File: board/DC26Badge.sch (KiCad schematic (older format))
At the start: 6 parts, among them U1 HT16K33-28

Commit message: Prototype schematic finished.
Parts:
- added C2: 4.7u, symbol DC26Badge-rescue:C_Small
- added C3, C4, C5: 0.1u, symbol DC26Badge-rescue:C_Small
- added D1, D2, D3: LED, symbol Device:LED
- added J1: PWR_HDR, symbol Connector_Generic:Conn_01x02
- added J2: PWR_CONN, symbol Connector_Generic:Conn_01x02
- added J3: VOLTMETER, symbol Connector_Generic:Conn_01x02
- added J4: AMMETER, symbol Connector_Generic:Conn_01x02
- added J5: Cortex_SWD, symbol Connector_Generic:Conn_02x05_Odd_Even
- added R1: 0.1, symbol Device:R_Shunt
- added R2, R3, R4, R5: 1k, symbol Device:R_Small
- added SW1: JOYSTICK, symbol dc26badge-custom:JOYSTICK
- added SW2: SW_Push, symbol Switch:SW_Push
- added TP1: PWRTP, symbol Connector_Specialized:Test_Point_2Pole
- added U2: BT832, symbol dc26badge-custom:BT832
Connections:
- net labels added: CTR, DN, LED1, LED2, LED3, LT, P_IN, RESET, RT, SWDCLK, SWDIO, UP
- wire segments 98 -> 183
- no-connect marks 1 -> 5
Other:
- moved on the sheet: C1

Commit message: First pass of prototype PCB layout.
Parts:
- removed D2, D3: LED, symbol Device:LED
- removed R4, R5: 1k, symbol Device:R_Small
- C2, C3, C4, C5: footprint (none) -> Capacitor_SMD:C_0603_1608Metric
- D1: footprint (none) -> LED_SMD:LED_0603_1608Metric
- J1, J3, J4: footprint (none) -> PinHeaders:Pin_Header_Straight_1x02_Pitch2.54mm
- J2: footprint (none) -> Connector_JST:JST_PH_S2B-PH-SM4-TB_1x02_P2.00mm_Horizontal
- J5: footprint (none) -> Connector_PinHeader_1.27mm:PinHeader_2x05_P1.27mm_Vertical_SMD
- R1: footprint (none) -> DC26badge:FC4T
- R2, R3: footprint (none) -> Resistor_SMD:R_0603_1608Metric
- SW1: footprint (none) -> DC26badge:JOYSTICK
- SW2: footprint (none) -> Button_Switch_SMD:SW_SPST_SKQG
- TP1: footprint (none) -> TestPoint:TestPoint_2Pads_Pitch2.54mm_Drill0.8mm
- U2: footprint (none) -> DC26badge:BT832
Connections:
- net labels removed: LED2, LED3
- wire segments 183 -> 173
- no-connect marks 5 -> 7
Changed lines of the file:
@@
 F 0 "U2" H 4500 3900 50  0000 C CNN
 F 1 "BT832" H 4025 5124 50  0000 C CNN
-F 2 "" H 3850 4050 50  0001 C CNN
+F 2 "DC26badge:BT832" H 3850 4050 50  0001 C CNN
 F 3 "" H 3850 4050 50  0001 C CNN
 	1    4050 4050
@@
 F 0 "J5" H 6850 3767 50  0000 C CNN
 F 1 "Cortex_SWD" H 6850 3676 50  0000 C CNN
-F 2 "" H 6800 3350 50  0001 C CNN
+F 2 "Connector_PinHeader_1.27mm:PinHeader_2x05_P1.27mm_Vertical_SMD" H 6800 3350 50  0001 C CNN
 F 3 "~" H 6800 3350 50  0001 C CNN
 	1    6800 3350
@@
 F 0 "SW1" H 4500 4700 50  0000 C CNN
 F 1 "JOYSTICK" H 4050 5324 50  0000 C CNN
-F 2 "" H 4050 5000 50  0001 C CNN
+F 2 "DC26badge:JOYSTICK" H 4050 5000 50  0001 C CNN
 F 3 "" H 4050 5000 50  0001 C CNN
 	1    4050 5000
@@
 	5000 5100 4700 5100
 Text Label 3000 3400 0    50   ~ 0
+UP
+Text Label 3000 3500 0    50   ~ 0
 CTR
-Text Label 3000 3500 0    50   ~ 0
-UP
 Text Label 3000 3600 0    50   ~ 0
 DN
@@
 L Connector_Generic:Conn_01x02 J1
 U 1 1 5AFF7E7C
-P 950 1050
-F 0 "J1" H 870 725 50  0000 C CNN
-F 1 "PWR_HDR" H 870 816 50  0000 C CNN
-F 2 "" H 950 1050 50  0001 C CNN
-F 3 "~" H 950 1050 50  0001 C CNN
-	1    950  1050
-	-1   0    0    1
+P 950 950
+F 0 "J1" H 870 1167 50  0000 C CNN
+F 1 "PWR_HDR" H 870 1076 50  0000 C CNN
+F 2 "PinHeaders:Pin_Header_Straight_1x02_Pitch2.54mm" H 950 950 50  0001 C CNN
+F 3 "~" H 950 950 50  0001 C CNN
+	1    950  950
+	-1   0    0    -1
 $EndComp
 $Comp
 L Connector_Generic:Conn_01x02 J2
 U 1 1 5AFF7F88
-P 950 1700
-F 0 "J2" H 870 1375 50  0000 C CNN
-F 1 "PWR_CONN" H 870 1466 50  0000 C CNN
-F 2 "" H 950 1700 50  0001 C CNN
-F 3 "~" H 950 1700 50  0001 C CNN
-	1    950  1700
-	-1   0    0    1
+P 950 1600
+F 0 "J2" H 870 1817 50  0000 C CNN
+F 1 "PWR_CONN" H 870 1726 50  0000 C CNN
+F 2 "Connector_JST:JST_PH_S2B-PH-SM4-TB_1x02_P2.00mm_Horizontal" H 950 1600 50  0001 C CNN
+F 3 "~" H 950 1600 50  0001 C CNN
+	1    950  1600
+	-1   0    0    -1
 $EndComp
 $Comp
 L Connector_Generic:Conn_01x02 J3
 U 1 1 5AFF811D
-P 950 2300
-F 0 "J3" H 870 1975 50  0000 C CNN
-F 1 "VOLTMETER" H 870 2066 50  0000 C CNN
-F 2 "" H 950 2300 50  0001 C CNN
-F 3 "~" H 950 2300 50  0001 C CNN
-	1    950  2300
-	-1   0    0    1
+P 950 2200
+F 0 "J3" H 870 2417 50  0000 C CNN
+F 1 "VOLTMETER" H 870 2326 50  0000 C CNN
+F 2 "PinHeaders:Pin_Header_Straight_1x02_Pitch2.54mm" H 950 2200 50  0001 C CNN
+F 3 "~" H 950 2200 50  0001 C CNN
+	1    950  2200
+	-1   0    0    -1
 $EndComp
 $Comp
@@
 F 0 "J4" H 870 2625 50  0000 C CNN
 F 1 "AMMETER" H 870 2716 50  0000 C CNN
-F 2 "" H 950 2950 50  0001 C CNN
+F 2 "PinHeaders:Pin_Header_Straight_1x02_Pitch2.54mm" H 950 2950 50  0001 C CNN
 F 3 "~" H 950 2950 50  0001 C CNN
 	1    950  2950
@@
 F 0 "R1" H 1362 2904 50  0000 R CNN
 F 1 "0.1" H 1362 2995 50  0000 R CNN
-F 2 "" V 1380 2950 50  0001 C CNN
+F 2 "DC26badge:FC4T" V 1380 2950 50  0001 C CNN
 F 3 "~" H 1450 2950 50  0001 C CNN
 	1    1450 2950
@@
 F 0 "C2" H 2242 1046 50  0000 L CNN
 F 1 "4.7u" H 2242 955 50  0000 L CNN
-F 2 "" H 2150 1000 50  0001 C CNN
+F 2 "Capacitor_SMD:C_0603_1608Metric" H 2150 1000 50  0001 C CNN
 F 3 "" H 2150 1000 50  0001 C CNN
 	1    2150 1000
@@
 F 0 "C3" H 2542 1046 50  0000 L CNN
 F 1 "0.1u" H 2542 955 50  0000 L CNN
-F 2 "" H 2450 1000 50  0001 C CNN
+F 2 "Capacitor_SMD:C_0603_1608Metric" H 2450 1000 50  0001 C CNN
 F 3 "" H 2450 1000 50  0001 C CNN
 	1    2450 1000
@@
 F 0 "C4" H 2842 1046 50  0000 L CNN
 F 1 "0.1u" H 2842 955 50  0000 L CNN
-F 2 "" H 2750 1000 50  0001 C CNN
+F 2 "Capacitor_SMD:C_0603_1608Metric" H 2750 1000 50  0001 C CNN
 F 3 "" H 2750 1000 50  0001 C CNN
 	1    2750 1000
@@
 F 0 "SW2" H 1800 4435 50  0000 C CNN
 F 1 "SW_Push" H 1800 4344 50  0000 C CNN
-F 2 "" H 1800 4350 50  0001 C CNN
+F 2 "Button_Switch_SMD:SW_SPST_SKQG" H 1800 4350 50  0001 C CNN
 F 3 "" H 1800 4350 50  0001 C CNN
 	1    1800 4150
@@
 F 0 "C5" H 1392 4396 50  0000 L CNN
 F 1 "0.1u" H 1392 4305 50  0000 L CNN
-F 2 "" H 1300 4350 50  0001 C CNN
+F 2 "Capacitor_SMD:C_0603_1608Metric" H 1300 4350 50  0001 C CNN
 F 3 "" H 1300 4350 50  0001 C CNN
 	1    1300 4350
@@
 F 0 "R3" H 1359 3996 50  0000 L CNN
 F 1 "1k" H 1359 3905 50  0000 L CNN
-F 2 "" H 1300 3950 50  0001 C CNN
+F 2 "Resistor_SMD:R_0603_1608Metric" H 1300 3950 50  0001 C CNN
 F 3 "~" H 1300 3950 50  0001 C CNN
 	1    1300 3950
@@
 F 0 "D1" V 988 5233 50  0000 R CNN
 F 1 "LED" V 897 5233 50  0000 R CNN
-F 2 "" H 950 5350 50  0001 C CNN
+F 2 "LED_SMD:LED_0603_1608Metric" H 950 5350 50  0001 C CNN
 F 3 "~" H 950 5350 50  0001 C CNN
 	1    950  5350
@@
 $EndComp
 $Comp
-L Device:LED D2
-U 1 1 5B0E1889
-P 1300 5350
-F 0 "D2" V 1338 5233 50  0000 R CNN
-F 1 "LED" V 1247 5233 50  0000 R CNN
-F 2 "" H 1300 5350 50  0001 C CNN
-F 3 "~" H 1300 5350 50  0001 C CNN
-	1    1300 5350
-	0    -1   -1   0
-$EndComp
-$Comp
-L Device:LED D3
-U 1 1 5B0E19A7
-P 1600 5350
-F 0 "D3" V 1638 5233 50  0000 R CNN
-F 1 "LED" V 1547 5233 50  0000 R CNN
-F 2 "" H 1600 5350 50  0001 C CNN
-F 3 "~" H 1600 5350 50  0001 C CNN
-	1    1600 5350
-	0    -1   -1   0
-$EndComp
-$Comp
 L power:VDD #PWR0103
 U 1 1 5B0E1C02
-P 1300 5100
-F 0 "#PWR0103" H 1300 4950 50  0001 C CNN
-F 1 "VDD" H 1317 5273 50  0000 C CNN
-F 2 "" H 1300 5100 50  0001 C CNN
-F 3 "" H 1300 5100 50  0001 C CNN
-	1    1300 5100
+P 950 5100
+F 0 "#PWR0103" H 950 4950 50  0001 C CNN
+F 1 "VDD" H 967 5273 50  0000 C CNN
+F 2 "" H 950 5100 50  0001 C CNN
+F 3 "" H 950 5100 50  0001 C CNN
+	1    950  5100
 	1    0    0    -1
 $EndComp
 Wire Wire Line
 	950  5200 950  5100
-Wire Wire Line
-	950  5100 1300 5100
-Wire Wire Line
-	1300 5200 1300 5100
-Connection ~ 1300 5100
-Wire Wire Line
-	1300 5100 1600 5100
-Wire Wire Line
-	1600 5100 1600 5200
 $Comp
 L Device:R_Small R2
@@
 F 0 "R2" H 1009 5796 50  0000 L CNN
 F 1 "1k" H 1009 5705 50  0000 L CNN
-F 2 "" H 950 5750 50  0001 C CNN
+F 2 "Resistor_SMD:R_0603_1608Metric" H 950 5750 50  0001 C CNN
 F 3 "~" H 950 5750 50  0001 C CNN
 	1    950  5750
 	1    0    0    -1
 $EndComp
-$Comp
-L Device:R_Small R4
-U 1 1 5B1339BD
-P 1300 5750
-F 0 "R4" H 1359 5796 50  0000 L CNN
-F 1 "1k" H 1359 5705 50  0000 L CNN
-F 2 "" H 1300 5750 50  0001 C CNN
-F 3 "~" H 1300 5750 50  0001 C CNN
-	1    1300 5750
-	1    0    0    -1
-$EndComp
-$Comp
-L Device:R_Small R5
-U 1 1 5B133A7E
-P 1600 5750
-F 0 "R5" H 1659 5796 50  0000 L CNN
-F 1 "1k" H 1659 5705 50  0000 L CNN
-F 2 "" H 1600 5750 50  0001 C CNN
-F 3 "~" H 1600 5750 50  0001 C CNN
-	1    1600 5750
-	1    0    0    -1
-$EndComp
 Wire Wire Line
 	950  5650 950  5500
 Wire Wire Line
-	1300 5500 1300 5650
-Wire Wire Line
-	1600 5650 1600 5500
-Wire Wire Line
 	950  5850 950  6100
-Wire Wire Line
-	1300 6100 1300 5850
-Wire Wire Line
-	1600 5850 1600 6100
-Text Label 950  6100 0    50   ~ 0
-LED1
-Text Label 1300 6100 0    50   ~ 0
-LED2
-Text Label 1600 6100 0    50   ~ 0
-LED3
 NoConn ~ 3300 3900
 Wire Wire Line
 	4750 3500 5000 3500
-Wire Wire Line
-	4750 3600 5000 3600
-Wire Wire Line
-	4750 3700 5000 3700
 Text Label 5000 3500 2    50   ~ 0
 LED1
-Text Label 5000 3600 2    50   ~ 0
-LED2
-Text Label 5000 3700 2    50   ~ 0
-LED3
 $Comp
 L Connector_Specialized:Test_Point_2Pole TP1
@@
 F 0 "TP1" H 2450 2245 50  0000 C CNN
 F 1 "PWRTP" H 2450 2154 50  0000 C CNN
-F 2 "" H 2450 2050 50  0001 C CNN
+F 2 "TestPoint:TestPoint_2Pads_Pitch2.54mm_Drill0.8mm" H 2450 2050 50  0001 C CNN
 F 3 "~" H 2450 2050 50  0001 C CNN
 	1    2450 2050
@@
 	2850 2200 2850 2050
 Connection ~ 2850 2050
+$Comp
+L power:GND #PWR0104
+U 1 1 5B1EF48E
+P 6400 3700
+F 0 "#PWR0104" H 6400 3450 50  0001 C CNN
+F 1 "GND" H 6405 3527 50  0000 C CNN
+F 2 "" H 6400 3700 50  0001 C CNN
+F 3 "" H 6400 3700 50  0001 C CNN
+	1    6400 3700
+	1    0    0    -1
+$EndComp
+NoConn ~ 4750 3700
+NoConn ~ 4750 3600
+Text Label 950  6100 0    50   ~ 0
+LED1
 $EndSCHEMATC

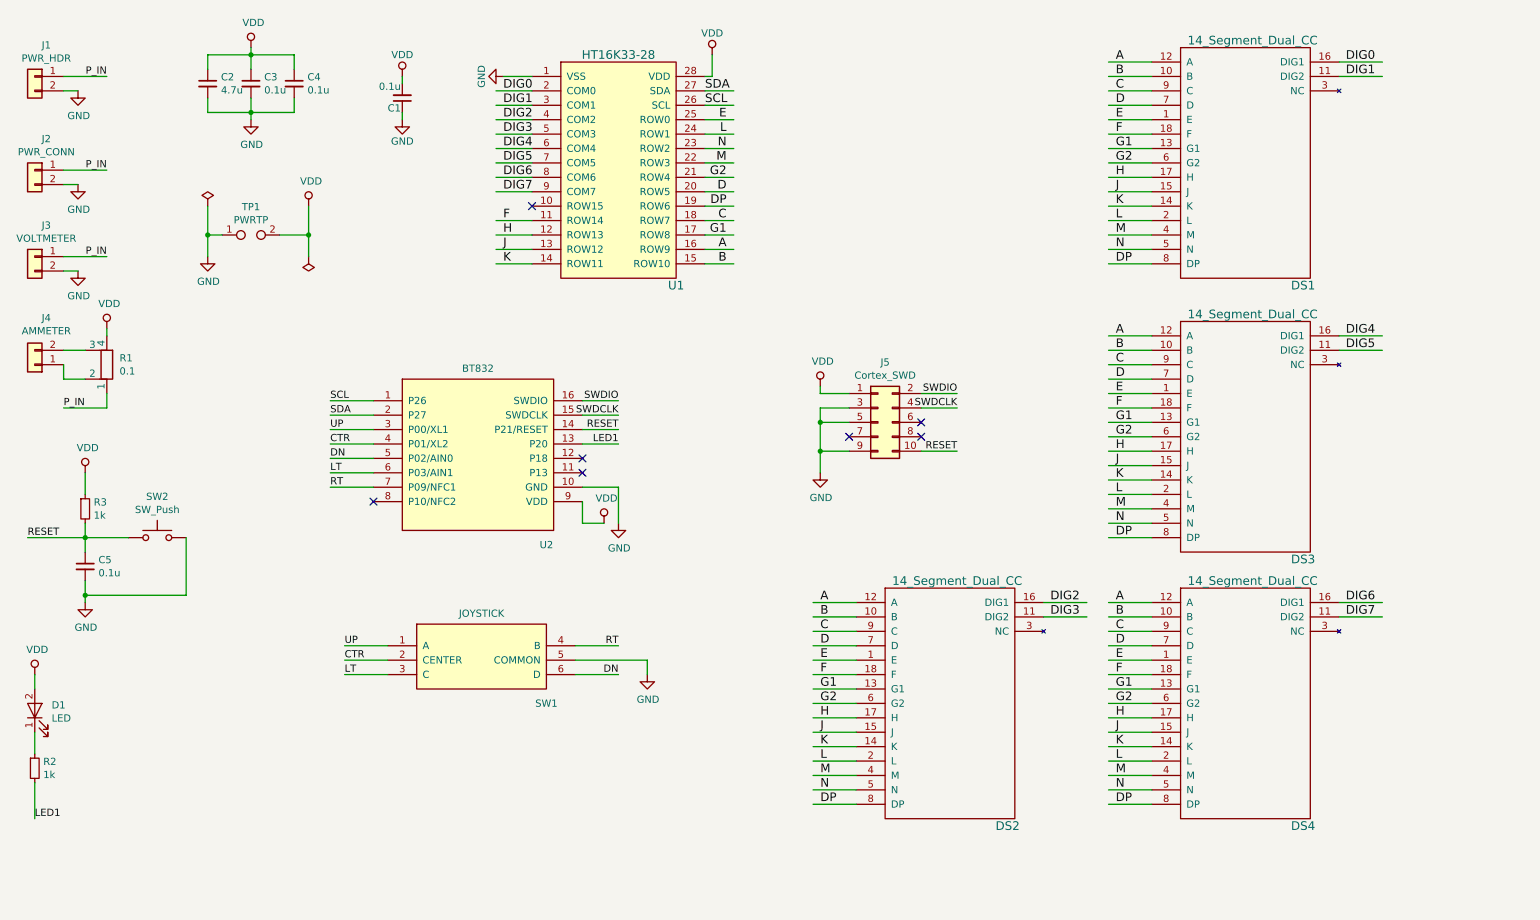
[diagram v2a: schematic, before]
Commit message: Do first circular board.
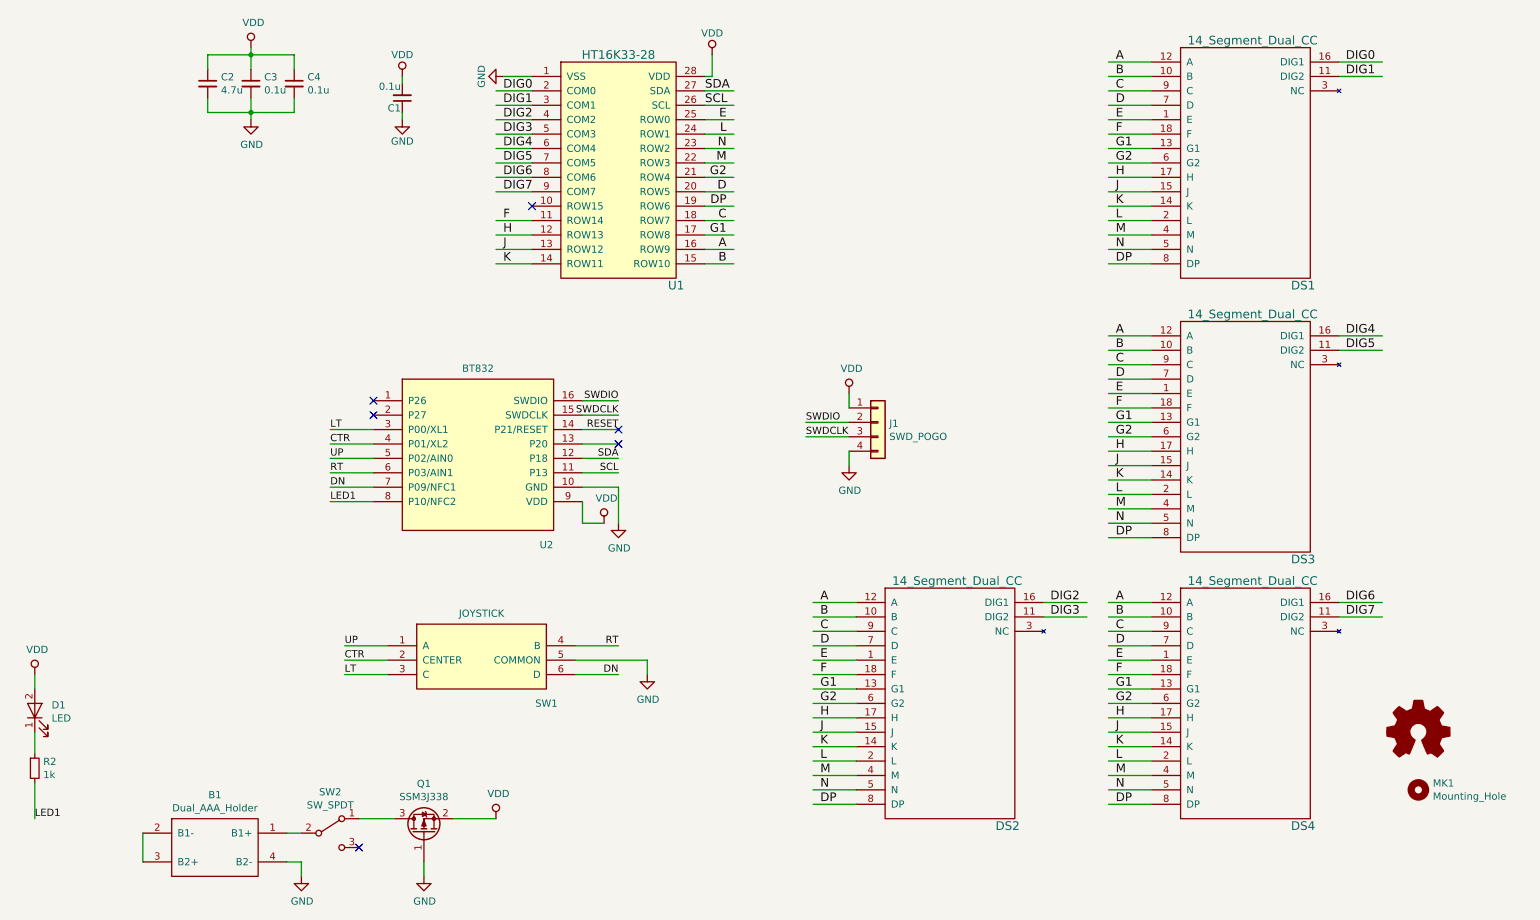
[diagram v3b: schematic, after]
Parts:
- removed C5: 0.1u, Capacitor_SMD:C_0603_1608Metric, symbol DC26Badge-rescue:C_Small
- removed J1: PWR_HDR, PinHeaders:Pin_Header_Straight_1x02_Pitch2.54mm, symbol Connector_Generic:Conn_01x02
- removed J2: PWR_CONN, Connector_JST:JST_PH_S2B-PH-SM4-TB_1x02_P2.00mm_Horizontal, symbol Connector_Generic:Conn_01x02
- removed J3: VOLTMETER, PinHeaders:Pin_Header_Straight_1x02_Pitch2.54mm, symbol Connector_Generic:Conn_01x02
- removed J4: AMMETER, PinHeaders:Pin_Header_Straight_1x02_Pitch2.54mm, symbol Connector_Generic:Conn_01x02
- removed J5: Cortex_SWD, Connector_PinHeader_1.27mm:PinHeader_2x05_P1.27mm_Vertical_SMD, symbol Connector_Generic:Conn_02x05_Odd_Even
- removed R1: 0.1, DC26badge:FC4T, symbol Device:R_Shunt
- removed R3: 1k, Resistor_SMD:R_0603_1608Metric, symbol Device:R_Small
- removed SW2: SW_Push, Button_Switch_SMD:SW_SPST_SKQG, symbol Switch:SW_Push
- removed TP1: PWRTP, TestPoint:TestPoint_2Pads_Pitch2.54mm_Drill0.8mm, symbol Connector_Specialized:Test_Point_2Pole
- added B1: Dual_AAA_Holder, DC26badge:Keystone_1022, symbol dc26badge-custom:Dual_AAA_Holder
- added J1: SWD_POGO, DC26badge:SWD_POGO, symbol Connector_Generic:Conn_01x04
- added MK1: Mounting_Hole, MountingHole:MountingHole_3.2mm_M3, symbol Mechanical:Mounting_Hole
- added Q1: SSM3J338, Package_TO_SOT_SMD:SOT-23_Handsoldering, symbol Device:Q_PMOS_GSD
- added SW2: SW_SPDT, DC26badge:JS102011SAQN, symbol Switch:SW_SPDT
- U1: footprint DC26badge:SOIC-28-300mil -> DC26badge:HT16K133
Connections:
- net labels removed: P_IN
- wire segments 173 -> 147
- no-connect marks 7 -> 6

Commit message: Fix up board.
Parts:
- added J2: SWD, Connector_PinHeader_1.27mm:PinHeader_2x05_P1.27mm_Vertical_SMD, symbol Connector_Generic:Conn_02x05_Odd_Even
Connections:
- wire segments 147 -> 157
- no-connect marks 6 -> 10
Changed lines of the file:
@@
 F 0 "#LOGO1" H 10550 5775 50  0001 C CNN
 F 1 "Logo_Open_Hardware_Small" H 10550 5275 50  0001 C CNN
-F 2 "" H 10550 5500 50  0001 C CNN
+F 2 "Symbol:OSHW-Logo2_7.3x6mm_SilkScreen" H 10550 5500 50  0001 C CNN
 F 3 "~" H 10550 5500 50  0001 C CNN
 	1    10550 5500
@@
 	3300 3900 3000 3900
 NoConn ~ 5000 3500
+$Comp
+L Connector_Generic:Conn_02x05_Odd_Even J2
+U 1 1 5B11E25C
+P 5650 3400
+F 0 "J2" H 5700 3817 50  0000 C CNN
+F 1 "SWD" H 5700 3726 50  0000 C CNN
+F 2 "Connector_PinHeader_1.27mm:PinHeader_2x05_P1.27mm_Vertical_SMD" H 5650 3400 50  0001 C CNN
+F 3 "~" H 5650 3400 50  0001 C CNN
+	1    5650 3400
+	1    0    0    -1
+$EndComp
+NoConn ~ 5450 3500
+NoConn ~ 5950 3600
+NoConn ~ 5950 3500
+NoConn ~ 5950 3400
+Wire Wire Line
+	5950 3200 6200 3200
+Wire Wire Line
+	5950 3300 6200 3300
+Wire Wire Line
+	5450 3200 5350 3200
+Wire Wire Line
+	5350 3200 5350 3000
+$Comp
+L power:VDD #PWR0101
+U 1 1 5B15EB46
+P 5350 3000
+F 0 "#PWR0101" H 5350 2850 50  0001 C CNN
+F 1 "VDD" H 5367 3173 50  0000 C CNN
+F 2 "" H 5350 3000 50  0001 C CNN
+F 3 "" H 5350 3000 50  0001 C CNN
+	1    5350 3000
+	1    0    0    -1
+$EndComp
+$Comp
+L power:GND #PWR0102
+U 1 1 5B15ED6F
+P 5350 3700
+F 0 "#PWR0102" H 5350 3450 50  0001 C CNN
+F 1 "GND" H 5355 3527 50  0000 C CNN
+F 2 "" H 5350 3700 50  0001 C CNN
+F 3 "" H 5350 3700 50  0001 C CNN
+	1    5350 3700
+	1    0    0    -1
+$EndComp
+Wire Wire Line
+	5450 3300 5350 3300
+Wire Wire Line
+	5350 3300 5350 3400
+Wire Wire Line
+	5450 3400 5350 3400
+Connection ~ 5350 3400
+Wire Wire Line
+	5350 3400 5350 3600
+Wire Wire Line
+	5450 3600 5350 3600
+Connection ~ 5350 3600
+Wire Wire Line
+	5350 3600 5350 3700
+Text Label 6200 3200 2    50   ~ 0
+SWDIO
+Text Label 6200 3300 2    50   ~ 0
+SWDCLK
 $EndSCHEMATC
